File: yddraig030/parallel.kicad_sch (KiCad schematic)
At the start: 4 parts

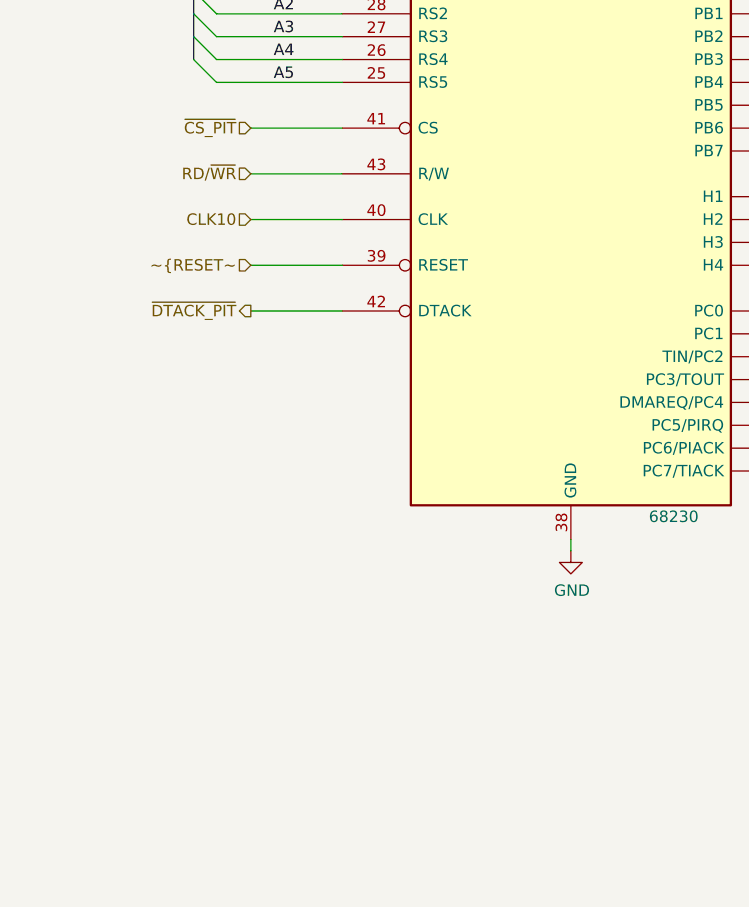
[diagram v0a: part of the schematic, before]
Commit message: More changes to the 030 board
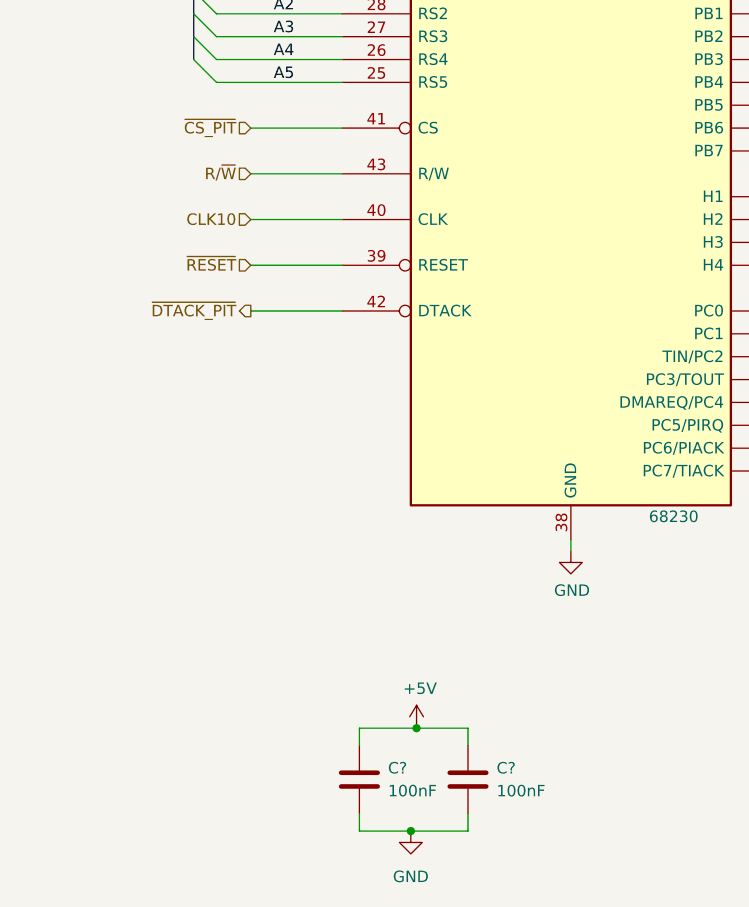
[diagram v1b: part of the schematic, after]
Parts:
- added C? (x2): 100nF, symbol Device:C
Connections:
- net +5V: now also C?.1, C?.1
- net GND: now also C?.2, C?.2
- net RD/~{WR} renamed R/~{W}
- net ~{RESET~ renamed ~{RESET}
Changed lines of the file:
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@@
   (junction (at 201.93 94.615) (diameter 0) (color 0 0 0 0)
+  )
+  (junction (at 100.965 161.29) (diameter 0) (color 0 0 0 0)
+  )
+  (junction (at 100.33 172.72) (diameter 0) (color 0 0 0 0)
   )
   (junction (at 201.93 109.855) (diameter 0) (color 0 0 0 0)
@@
     (stroke (width 0) (type default) (color 0 0 0 0))
   )
+  (wire (pts (xy 106.68 161.29) (xy 106.68 163.195))
+    (stroke (width 0) (type default) (color 0 0 0 0))
+  )
   (wire (pts (xy 82.55 114.935) (xy 92.71 114.935))
     (stroke (width 0) (type default) (color 0 0 0 0))
@@
     (stroke (width 0) (type default) (color 0 0 0 0))
   )
+  (wire (pts (xy 106.68 170.815) (xy 106.68 172.72))
+    (stroke (width 0) (type default) (color 0 0 0 0))
+  )
   (bus (pts (xy 76.2 64.135) (xy 76.2 66.675))
     (stroke (width 0) (type default) (color 0 0 0 0))
   )
+  (wire (pts (xy 94.615 170.815) (xy 94.615 172.72))
+    (stroke (width 0) (type default) (color 0 0 0 0))
+  )
   (wire (pts (xy 182.88 97.155) (xy 204.47 97.155))
     (stroke (width 0) (type default) (color 0 0 0 0))
@@
     (stroke (width 0) (type default) (color 0 0 0 0))
   )
+  (wire (pts (xy 100.965 161.29) (xy 106.68 161.29))
+    (stroke (width 0) (type default) (color 0 0 0 0))
+  )
   (wire (pts (xy 143.51 61.595) (xy 170.18 61.595))
     (stroke (width 0) (type default) (color 0 0 0 0))
@@
     (stroke (width 0) (type default) (color 0 0 0 0))
   )
+  (wire (pts (xy 94.615 161.29) (xy 100.965 161.29))
+    (stroke (width 0) (type default) (color 0 0 0 0))
+  )
+  (wire (pts (xy 94.615 172.72) (xy 100.33 172.72))
+    (stroke (width 0) (type default) (color 0 0 0 0))
+  )
+  (wire (pts (xy 94.615 161.29) (xy 94.615 163.195))
+    (stroke (width 0) (type default) (color 0 0 0 0))
+  )
   (wire (pts (xy 143.51 109.855) (xy 180.34 109.855))
     (stroke (width 0) (type default) (color 0 0 0 0))
@@
   )
   (wire (pts (xy 162.56 81.915) (xy 162.56 69.215))
+    (stroke (width 0) (type default) (color 0 0 0 0))
+  )
+  (wire (pts (xy 100.33 172.72) (xy 106.68 172.72))
     (stroke (width 0) (type default) (color 0 0 0 0))
   )
@@
     (effects (font (size 1.27 1.27)) (justify right))
   )
-  (hierarchical_label "RD{slash}~{WR}" (shape input) (at 82.55 99.695 180)
+  (hierarchical_label "R{slash}~{W}" (shape input) (at 82.55 99.695 180)
     (effects (font (size 1.27 1.27)) (justify right))
   )
@@
     (effects (font (size 1.27 1.27)) (justify left))
   )
-  (hierarchical_label "~{RESET~" (shape input) (at 82.55 109.855 180)
+  (hierarchical_label "~{RESET}" (shape input) (at 82.55 109.855 180)
     (effects (font (size 1.27 1.27)) (justify right))
   )
@@
     )
     (property "Datasheet" "" (id 3) (at 201.93 121.285 0)
+      (effects (font (size 1.27 1.27)) hide)
+    )
+    (pin "1")
+  )
+  (symbol (lib_id "power:+5V") (at 100.965 161.29 0) (unit 1)
+    (in_bom yes) (on_board yes)
+    (property "Reference" "#PWR?" (id 0) (at 100.965 165.1 0)
+      (effects (font (size 1.27 1.27)) hide)
+    )
+    (property "Value" "+5V" (id 1) (at 101.346 156.8958 0))
+    (property "Footprint" "" (id 2) (at 100.965 161.29 0)
+      (effects (font (size 1.27 1.27)) hide)
+    )
+    (property "Datasheet" "" (id 3) (at 100.965 161.29 0)
       (effects (font (size 1.27 1.27)) hide)
     )
@@
     (pin "8")
   )
+  (symbol (lib_id "power:GND") (at 100.33 172.72 0) (unit 1)
+    (in_bom yes) (on_board yes) (fields_autoplaced)
+    (property "Reference" "#PWR?" (id 0) (at 100.33 179.07 0)
+      (effects (font (size 1.27 1.27)) hide)
+    )
+    (property "Value" "GND" (id 1) (at 100.33 177.8 0))
+    (property "Footprint" "" (id 2) (at 100.33 172.72 0)
+      (effects (font (size 1.27 1.27)) hide)
+    )
+    (property "Datasheet" "" (id 3) (at 100.33 172.72 0)
+      (effects (font (size 1.27 1.27)) hide)
+    )
+    (pin "1")
+  )
   (symbol (lib_id "Device:R") (at 166.37 53.975 90) (unit 1)
     (in_bom yes) (on_board yes)
@@
     )
     (pin "1")
+  )
+  (symbol (lib_id "Device:C") (at 106.68 167.005 0) (unit 1)
+    (in_bom yes) (on_board yes) (fields_autoplaced)
+    (property "Reference" "C?" (id 0) (at 109.855 165.7349 0)
+      (effects (font (size 1.27 1.27)) (justify left))
+    )
+    (property "Value" "100nF" (id 1) (at 109.855 168.2749 0)
+      (effects (font (size 1.27 1.27)) (justify left))
+    )
+    (property "Footprint" "" (id 2) (at 107.6452 170.815 0)
+      (effects (font (size 1.27 1.27)) hide)
+    )
+    (property "Datasheet" "~" (id 3) (at 106.68 167.005 0)
+      (effects (font (size 1.27 1.27)) hide)
+    )
+    (pin "1")
+    (pin "2")
   )
   (symbol (lib_id "power:GND") (at 184.785 155.575 0) (unit 1)
@@
     (pin "1")
   )
+  (symbol (lib_id "Device:C") (at 94.615 167.005 0) (unit 1)
+    (in_bom yes) (on_board yes) (fields_autoplaced)
+    (property "Reference" "C?" (id 0) (at 97.79 165.7349 0)
+      (effects (font (size 1.27 1.27)) (justify left))
+    )
+    (property "Value" "100nF" (id 1) (at 97.79 168.2749 0)
+      (effects (font (size 1.27 1.27)) (justify left))
+    )
+    (property "Footprint" "" (id 2) (at 95.5802 170.815 0)
+      (effects (font (size 1.27 1.27)) hide)
+    )
+    (property "Datasheet" "~" (id 3) (at 94.615 167.005 0)
+      (effects (font (size 1.27 1.27)) hide)
+    )
+    (pin "1")
+    (pin "2")
+  )
   (symbol (lib_id "power:GND") (at 118.11 141.605 0) (unit 1)

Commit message: ddraig030 schematic done
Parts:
- gave numbers to parts that had none: 6
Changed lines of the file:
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@@
   (symbol (lib_id "power:GND") (at 201.93 121.285 0) (unit 1)
     (in_bom yes) (on_board yes)
-    (property "Reference" "#PWR?" (id 0) (at 201.93 127.635 0)
+    (property "Reference" "#PWR01508" (id 0) (at 201.93 127.635 0)
       (effects (font (size 1.27 1.27)) hide)
     )
@@
   (symbol (lib_id "power:+5V") (at 100.965 161.29 0) (unit 1)
     (in_bom yes) (on_board yes)
-    (property "Reference" "#PWR?" (id 0) (at 100.965 165.1 0)
+    (property "Reference" "#PWR01502" (id 0) (at 100.965 165.1 0)
       (effects (font (size 1.27 1.27)) hide)
     )
@@
   (symbol (lib_id "Connector_Generic:Conn_01x08") (at 191.77 142.875 0) (unit 1)
     (in_bom yes) (on_board yes) (fields_autoplaced)
-    (property "Reference" "J?" (id 0) (at 194.31 142.8749 0)
+    (property "Reference" "J1501" (id 0) (at 194.31 142.8749 0)
       (effects (font (size 1.27 1.27)) (justify left))
     )
@@
   (symbol (lib_id "power:GND") (at 100.33 172.72 0) (unit 1)
     (in_bom yes) (on_board yes) (fields_autoplaced)
-    (property "Reference" "#PWR?" (id 0) (at 100.33 179.07 0)
+    (property "Reference" "#PWR01501" (id 0) (at 100.33 179.07 0)
       (effects (font (size 1.27 1.27)) hide)
     )
@@
   (symbol (lib_id "Device:R") (at 166.37 53.975 90) (unit 1)
     (in_bom yes) (on_board yes)
-    (property "Reference" "R?" (id 0) (at 166.37 48.7172 90))
+    (property "Reference" "R1501" (id 0) (at 166.37 48.7172 90))
     (property "Value" "1K" (id 1) (at 166.37 51.0286 90))
     (property "Footprint" "Resistor_THT:R_Axial_DIN0207_L6.3mm_D2.5mm_P10.16mm_Horizontal" (id 2) (at 166.37 55.753 90)
@@
   (symbol (lib_id "power:+5V") (at 184.785 132.08 0) (unit 1)
     (in_bom yes) (on_board yes)
-    (property "Reference" "#PWR?" (id 0) (at 184.785 135.89 0)
+    (property "Reference" "#PWR01506" (id 0) (at 184.785 135.89 0)
       (effects (font (size 1.27 1.27)) hide)
     )
@@
   (symbol (lib_id "Device:C") (at 106.68 167.005 0) (unit 1)
     (in_bom yes) (on_board yes) (fields_autoplaced)
-    (property "Reference" "C?" (id 0) (at 109.855 165.7349 0)
+    (property "Reference" "C1502" (id 0) (at 109.855 165.7349 0)
       (effects (font (size 1.27 1.27)) (justify left))
     )
@@
   (symbol (lib_id "power:GND") (at 184.785 155.575 0) (unit 1)
     (in_bom yes) (on_board yes)
-    (property "Reference" "#PWR?" (id 0) (at 184.785 161.925 0)
+    (property "Reference" "#PWR01507" (id 0) (at 184.785 161.925 0)
       (effects (font (size 1.27 1.27)) hide)
     )
@@
   (symbol (lib_id "Interface:68230") (at 118.11 94.615 0) (unit 1)
     (in_bom yes) (on_board yes)
-    (property "Reference" "U?" (id 0) (at 132.08 51.435 0))
+    (property "Reference" "U1501" (id 0) (at 132.08 51.435 0))
     (property "Value" "68230" (id 1) (at 129.54 137.795 0))
     (property "Footprint" "Package_DIP:DIP-48_W15.24mm_Socket" (id 2) (at 118.11 94.615 0)
@@
   (symbol (lib_id "power:+5V") (at 118.11 46.355 0) (unit 1)
     (in_bom yes) (on_board yes)
-    (property "Reference" "#PWR?" (id 0) (at 118.11 50.165 0)
+    (property "Reference" "#PWR01503" (id 0) (at 118.11 50.165 0)
       (effects (font (size 1.27 1.27)) hide)
     )
@@
   (symbol (lib_id "Device:C") (at 94.615 167.005 0) (unit 1)
     (in_bom yes) (on_board yes) (fields_autoplaced)
-    (property "Reference" "C?" (id 0) (at 97.79 165.7349 0)
+    (property "Reference" "C1501" (id 0) (at 97.79 165.7349 0)
       (effects (font (size 1.27 1.27)) (justify left))
     )
@@
   (symbol (lib_id "power:GND") (at 118.11 141.605 0) (unit 1)
     (in_bom yes) (on_board yes)
-    (property "Reference" "#PWR?" (id 0) (at 118.11 147.955 0)
+    (property "Reference" "#PWR01504" (id 0) (at 118.11 147.955 0)
       (effects (font (size 1.27 1.27)) hide)
     )
@@
   (symbol (lib_id "power:+5V") (at 160.02 51.435 0) (unit 1)
     (in_bom yes) (on_board yes)
-    (property "Reference" "#PWR?" (id 0) (at 160.02 55.245 0)
+    (property "Reference" "#PWR01505" (id 0) (at 160.02 55.245 0)
       (effects (font (size 1.27 1.27)) hide)
     )
@@
   (symbol (lib_id "Connector:DB25_Female_MountingHoles") (at 212.09 81.915 0) (unit 1)
     (in_bom yes) (on_board yes)
-    (property "Reference" "J?" (id 0) (at 216.662 81.8642 0)
-      (effects (font (size 1.27 1.27)) (justify left))
-    )
+    (property "Reference" "J1502" (id 0) (at 216.662 81.8642 0)
+      (effects (font (size 1.27 1.27)) (justify left))
+    )
